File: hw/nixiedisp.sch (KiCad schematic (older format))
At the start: 55 parts, among them J1 12VDC IN, J2 USB_B_Micro, J3 AVR-ISP-6, J4 pwr sw, Q1 MMBTA55, Q2 IRF540N, U1 ATmega328P-AU, U10 IN14, U11 IN14, U12 IN14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

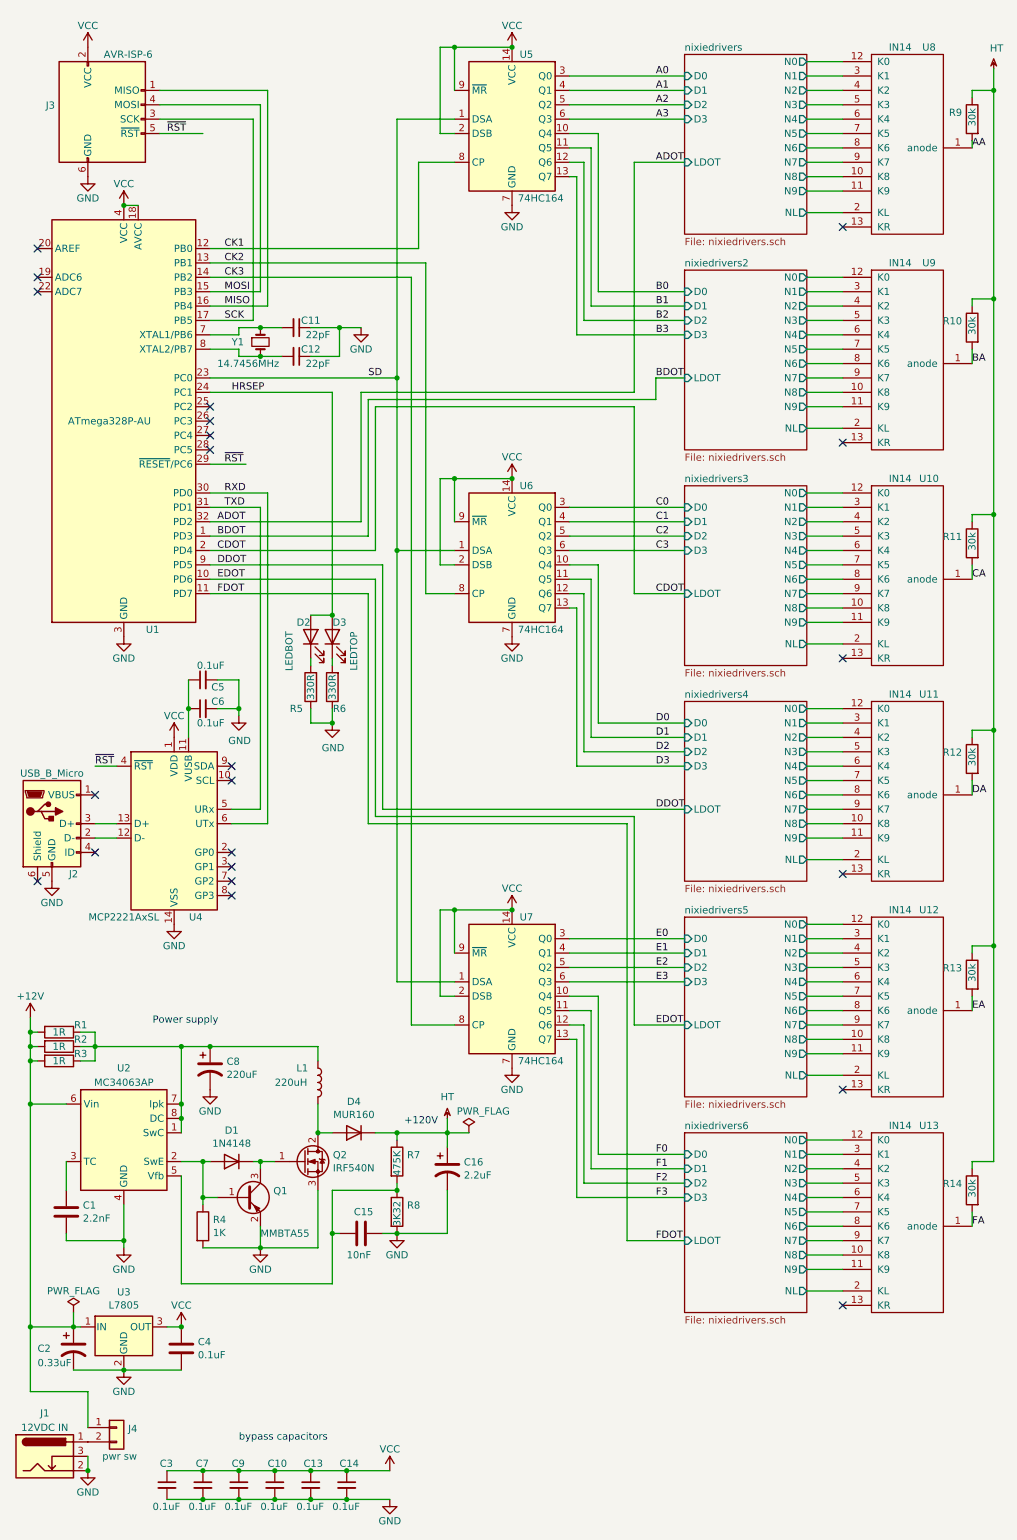
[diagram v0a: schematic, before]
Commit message: added RTC to the schematic
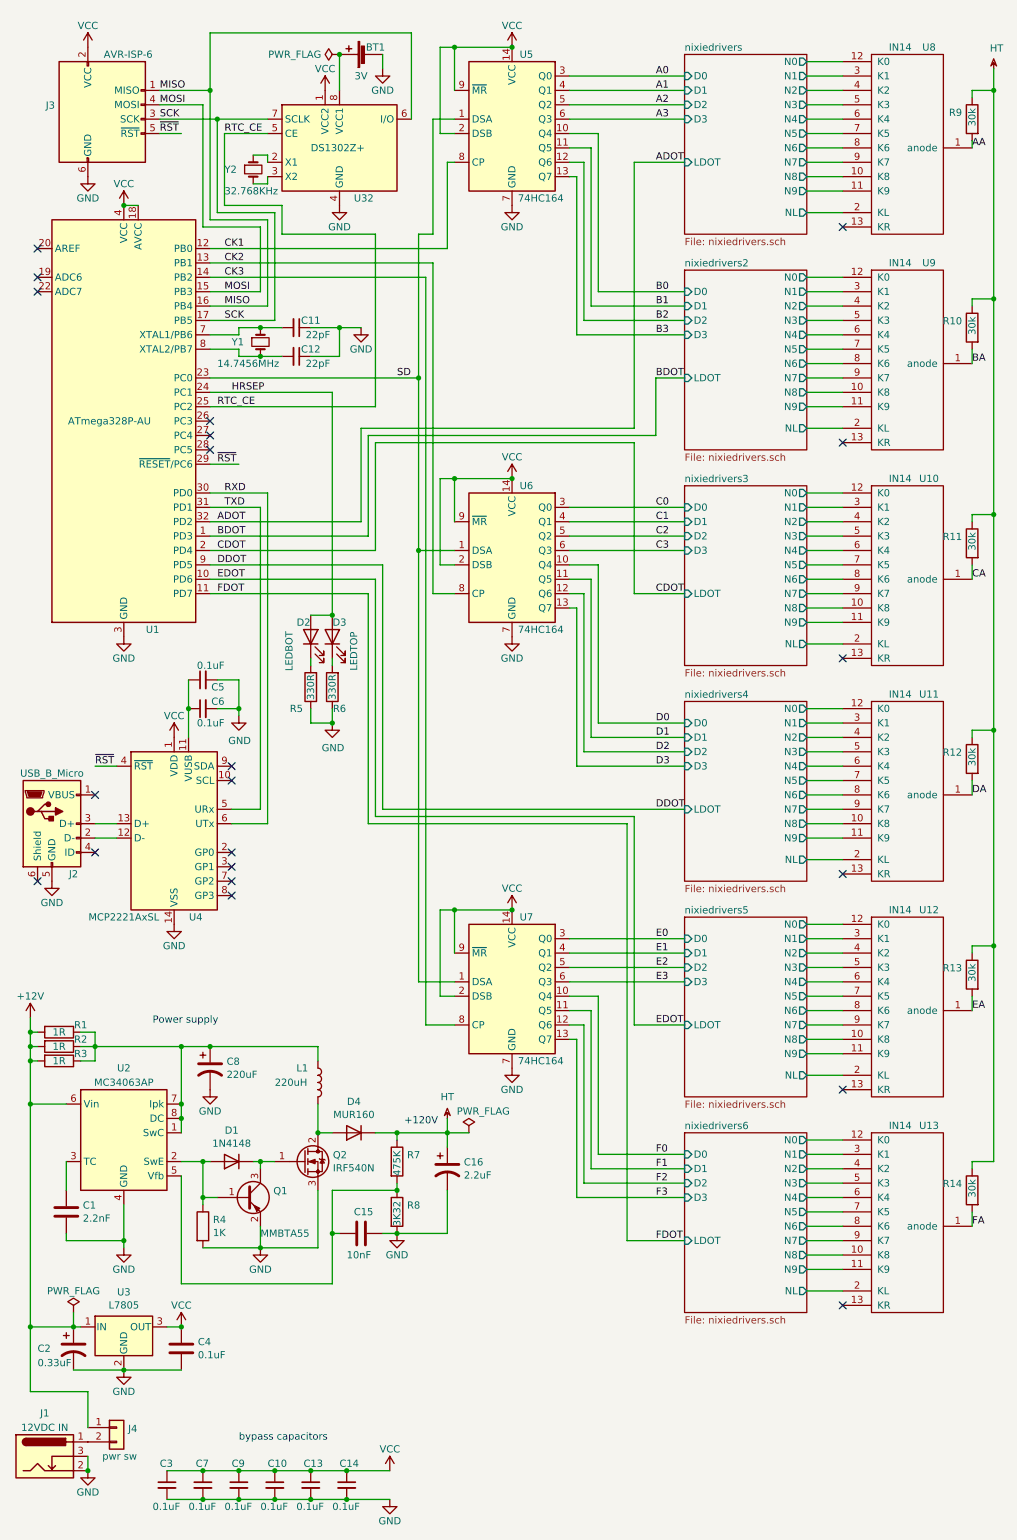
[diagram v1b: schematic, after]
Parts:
- added BT1: 3V, Battery:BatteryHolder_Keystone_1060_1x2032, symbol Device:Battery_Cell
- added U32: DS1302Z+, Package_SO:SOIC-8_3.9x4.9mm_P1.27mm, symbol Timer_RTC:DS1302Z+
- added Y2: 32.768KHz, Crystal:Crystal_SMD_2012-2Pin_2.0x1.2mm_HandSoldering, symbol Device:Crystal_Small
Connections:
- net GND: now also BT1.2 (-), U32.4 (GND)
- net MISO: now also U32.6 (I/O)
- net SCK: now also U32.7 (SCLK)
- net VCC: now also U32.1 (VCC2)
- net RTC_CE: now reaches U1.25 (PC2)
- net RTC_CE: now also U32.5 (CE)
- new net: U32.2 (X1), Y2.1
- new net: U32.3 (X2), Y2.2
- new net: BT1.1 (+), U32.8 (VCC1)
- no-connect marks 22 -> 21
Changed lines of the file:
@@
 Text Label 2150 2650 0    50   ~ 0
 MISO
-Wire Wire Line
-	2050 2750 2350 2750
 Text Label 2150 2750 0    50   ~ 0
 SCK
@@
 $EndComp
 Wire Wire Line
-	1700 1150 2450 1150
-Wire Wire Line
-	2450 1150 2450 2650
-Wire Wire Line
 	2050 2650 2450 2650
 Wire Wire Line
-	1700 1250 2400 1250
-Wire Wire Line
-	2400 1250 2400 2550
-Wire Wire Line
 	2050 2550 2400 2550
 Wire Wire Line
-	1700 1350 2350 1350
-Wire Wire Line
-	2350 1350 2350 2750
-Wire Wire Line
-	1700 1450 2000 1450
-Text Label 1750 1450 0    50   ~ 0
+	1700 1450 1850 1450
+Text Label 1700 1450 0    50   ~ 0
 ~RST
-Text Label 2150 3750 0    50   ~ 0
+Text Label 2100 3750 0    50   ~ 0
 ~RST
 $Comp
@@
 $EndComp
 Wire Wire Line
-	2050 2250 3500 2250
-Wire Wire Line
-	3500 2250 3500 1650
-Wire Wire Line
-	3500 1650 3750 1650
-Wire Wire Line
-	2050 2350 3550 2350
-Wire Wire Line
-	3550 2350 3550 4650
-Wire Wire Line
-	3550 4650 3750 4650
-Wire Wire Line
-	2050 2450 3450 2450
-Wire Wire Line
-	3450 2450 3450 7650
-Wire Wire Line
-	3450 7650 3750 7650
+	2050 2250 3700 2250
+Wire Wire Line
+	3700 2250 3700 1650
+Wire Wire Line
+	3700 1650 3750 1650
+Wire Wire Line
+	3600 2350 3600 4650
+Wire Wire Line
+	3600 4650 3750 4650
+Wire Wire Line
+	2050 2450 3550 2450
+Wire Wire Line
+	3550 2450 3550 7650
+Wire Wire Line
+	3550 7650 3750 7650
 Text Label 2150 2250 0    50   ~ 0
 CK1
@@
 TXD
 Wire Wire Line
-	3350 3150 3350 1350
-Wire Wire Line
-	3350 1350 3750 1350
-Wire Wire Line
-	3350 3150 3350 4350
-Wire Wire Line
-	3350 4350 3750 4350
-Connection ~ 3350 3150
-Wire Wire Line
-	3350 4350 3350 7350
-Wire Wire Line
-	3350 7350 3750 7350
-Connection ~ 3350 4350
-Text Label 3150 3150 0    50   ~ 0
+	3500 3150 3500 2150
+Wire Wire Line
+	3500 3150 3500 4350
+Wire Wire Line
+	3500 4350 3750 4350
+Connection ~ 3500 3150
+Wire Wire Line
+	3500 4350 3500 7350
+Wire Wire Line
+	3500 7350 3750 7350
+Connection ~ 3500 4350
+Text Label 3350 3150 0    50   ~ 0
 SD
 Wire Wire Line
@@
 Connection ~ 3750 6850
 Wire Wire Line
-	2050 3150 3350 3150
+	2050 3150 3500 3150
 Wire Wire Line
 	2950 2800 3100 2800
@@
 FDOT
 Wire Wire Line
-	3100 4150 3100 3250
-Wire Wire Line
-	3100 3250 5000 3250
-Wire Wire Line
-	5000 3250 5000 1650
+	3100 4150 3100 3500
+Wire Wire Line
+	3100 3500 5000 3500
+Wire Wire Line
+	5000 3500 5000 1650
 Wire Wire Line
 	5000 1650 5350 1650
@@
 	2050 4150 3100 4150
 Wire Wire Line
-	3150 4250 3150 3300
-Wire Wire Line
-	3150 3300 5150 3300
-Wire Wire Line
-	5150 3300 5150 3150
+	3150 4250 3150 3550
+Wire Wire Line
+	3150 3550 5150 3550
+Wire Wire Line
+	5150 3550 5150 3150
 Wire Wire Line
 	2050 4250 3150 4250
 Wire Wire Line
-	3200 4350 3200 3350
-Wire Wire Line
-	3200 3350 5000 3350
-Wire Wire Line
-	5000 3350 5000 4650
+	3200 4350 3200 3600
+Wire Wire Line
+	3200 3600 5000 3600
+Wire Wire Line
+	5000 3600 5000 4650
 Wire Wire Line
 	5000 4650 5350 4650
@@
 	2050 3950 2450 3950
 Wire Wire Line
-	2050 3750 2300 3750
+	2050 3750 2250 3750
 $Comp
 L Device:C_Small C6
@@
 	1    0    0    -1
 $EndComp
-NoConn ~ 2050 3350
 NoConn ~ 2050 3450
 NoConn ~ 2050 3550
@@
 Text Label 7350 9050 0    50   ~ 0
 FA
+$Comp
+L Timer_RTC:DS1302Z+ U32
+U 1 1 623FA4BC
+P 2950 1550
+F 0 "U32" H 3050 1200 50  0000 L CNN
+F 1 "DS1302Z+" H 2750 1550 50  0000 L CNN
+F 2 "Package_SO:SOIC-8_3.9x4.9mm_P1.27mm" H 2950 1050 50  0001 C CNN
+F 3 "https://datasheets.maximintegrated.com/en/ds/DS1302.pdf" H 2950 1550 50  0001 C CNN
+	1    2950 1550
+	1    0    0    -1
+$EndComp
+Wire Wire Line
+	2350 1800 2450 1800
+$Comp
+L power:GND #PWR0138
+U 1 1 62634E4F
+P 2950 1950
+F 0 "#PWR0138" H 2950 1700 50  0001 C CNN
+F 1 "GND" H 2950 1800 50  0000 C CNN
+F 2 "" H 2950 1950 50  0001 C CNN
+F 3 "" H 2950 1950 50  0001 C CNN
+	1    2950 1950
+	1    0    0    -1
+$EndComp
+Wire Wire Line
+	3450 1350 3450 750
+Wire Wire Line
+	3450 750  2050 750
+Wire Wire Line
+	1700 1350 2100 1350
+Wire Wire Line
+	2450 1800 2450 1750
+$Comp
+L Device:Crystal_Small Y2
+U 1 1 623FC7B6
+P 2350 1700
+F 0 "Y2" V 2350 1500 50  0000 L CNN
+F 1 "32.768KHz" V 2500 1500 50  0000 L CNN
+F 2 "Crystal:Crystal_SMD_2012-2Pin_2.0x1.2mm_HandSoldering" H 2350 1700 50  0001 C CNN
+F 3 "~" H 2350 1700 50  0001 C CNN
+F 4 "6pF" H 2350 1700 50  0001 C CNN "load"
+	1    2350 1700
+	0    1    1    0
+$EndComp
+Wire Wire Line
+	2350 1600 2450 1600
+Wire Wire Line
+	2450 1600 2450 1650
+Wire Wire Line
+	3500 2150 3600 2150
+Wire Wire Line
+	3600 2150 3600 1350
+Wire Wire Line
+	3600 1350 3750 1350
+Wire Wire Line
+	2400 2550 2400 2100
+Wire Wire Line
+	2400 2100 2000 2100
+Wire Wire Line
+	2000 2100 2000 1250
+Wire Wire Line
+	2000 1250 1700 1250
+Wire Wire Line
+	2450 2650 2450 2050
+Wire Wire Line
+	2450 2050 2050 2050
+Wire Wire Line
+	2050 2050 2050 1150
+Wire Wire Line
+	2050 1150 1700 1150
+Wire Wire Line
+	2050 2350 3600 2350
+Wire Wire Line
+	2500 2750 2500 2000
+Wire Wire Line
+	2500 2000 2100 2000
+Wire Wire Line
+	2100 2000 2100 1350
+Wire Wire Line
+	2050 2750 2500 2750
+Connection ~ 2100 1350
+Wire Wire Line
+	2100 1350 2450 1350
+$Comp
+L power:VCC #PWR0137
+U 1 1 62891898
+P 2850 1150
+F 0 "#PWR0137" H 2850 1000 50  0001 C CNN
+F 1 "VCC" H 2850 1300 50  0000 C CNN
+F 2 "" H 2850 1150 50  0001 C CNN
+F 3 "" H 2850 1150 50  0001 C CNN
+	1    2850 1150
+	1    0    0    -1
+$EndComp
+$Comp
+L Device:Battery_Cell BT1
+U 1 1 62892D7C
+P 3150 900
+F 0 "BT1" V 3200 850 50  0000 C CNN
+F 1 "3V" V 3000 950 50  0000 C CNN
+F 2 "Battery:BatteryHolder_Keystone_1060_1x2032" V 3150 960 50  0001 C CNN
+F 3 "~" V 3150 960 50  0001 C CNN
+	1    3150 900
+	0    -1   -1   0
+$EndComp
+$Comp
+L power:GND #PWR0139
+U 1 1 6289505D
+P 3250 1000
+F 0 "#PWR0139" H 3250 750 50  0001 C CNN
+F 1 "GND" H 3250 850 50  0000 C CNN
+F 2 "" H 3250 1000 50  0001 C CNN
+F 3 "" H 3250 1000 50  0001 C CNN
+	1    3250 1000
+	1    0    0    -1
+$EndComp
+Wire Wire Line
+	3250 900  3250 1000
+Wire Wire Line
+	2950 900  2950 1150
+Text Label 2100 3350 0    50   ~ 0
+RTC_CE
+Wire Wire Line
+	2450 1450 2150 1450
+Text Label 2150 1450 0    50   ~ 0
+RTC_CE
+Wire Wire Line
+	3200 3350 3200 2150
+Wire Wire Line
+	3200 2150 2550 2150
+Wire Wire Line
+	2550 2150 2550 1950
+Wire Wire Line
+	2550 1950 2150 1950
+Wire Wire Line
+	2150 1950 2150 1450
+Wire Wire Line
+	2050 3350 3200 3350
+Wire Wire Line
+	2050 750  2050 1150
+Connection ~ 2050 1150
+Text Label 1700 1150 0    50   ~ 0
+MISO
+Text Label 1700 1250 0    50   ~ 0
+MOSI
+Text Label 1700 1350 0    50   ~ 0
+SCK
+$Comp
+L power:PWR_FLAG #FLG0103
+U 1 1 62B59C57
+P 2950 900
+F 0 "#FLG0103" H 2950 975 50  0001 C CNN
+F 1 "PWR_FLAG" V 2950 1027 50  0000 L CNN
+F 2 "" H 2950 900 50  0001 C CNN
+F 3 "~" H 2950 900 50  0001 C CNN
+	1    2950 900
+	0    -1   -1   0
+$EndComp
+Connection ~ 2950 900
 $EndSCHEMATC

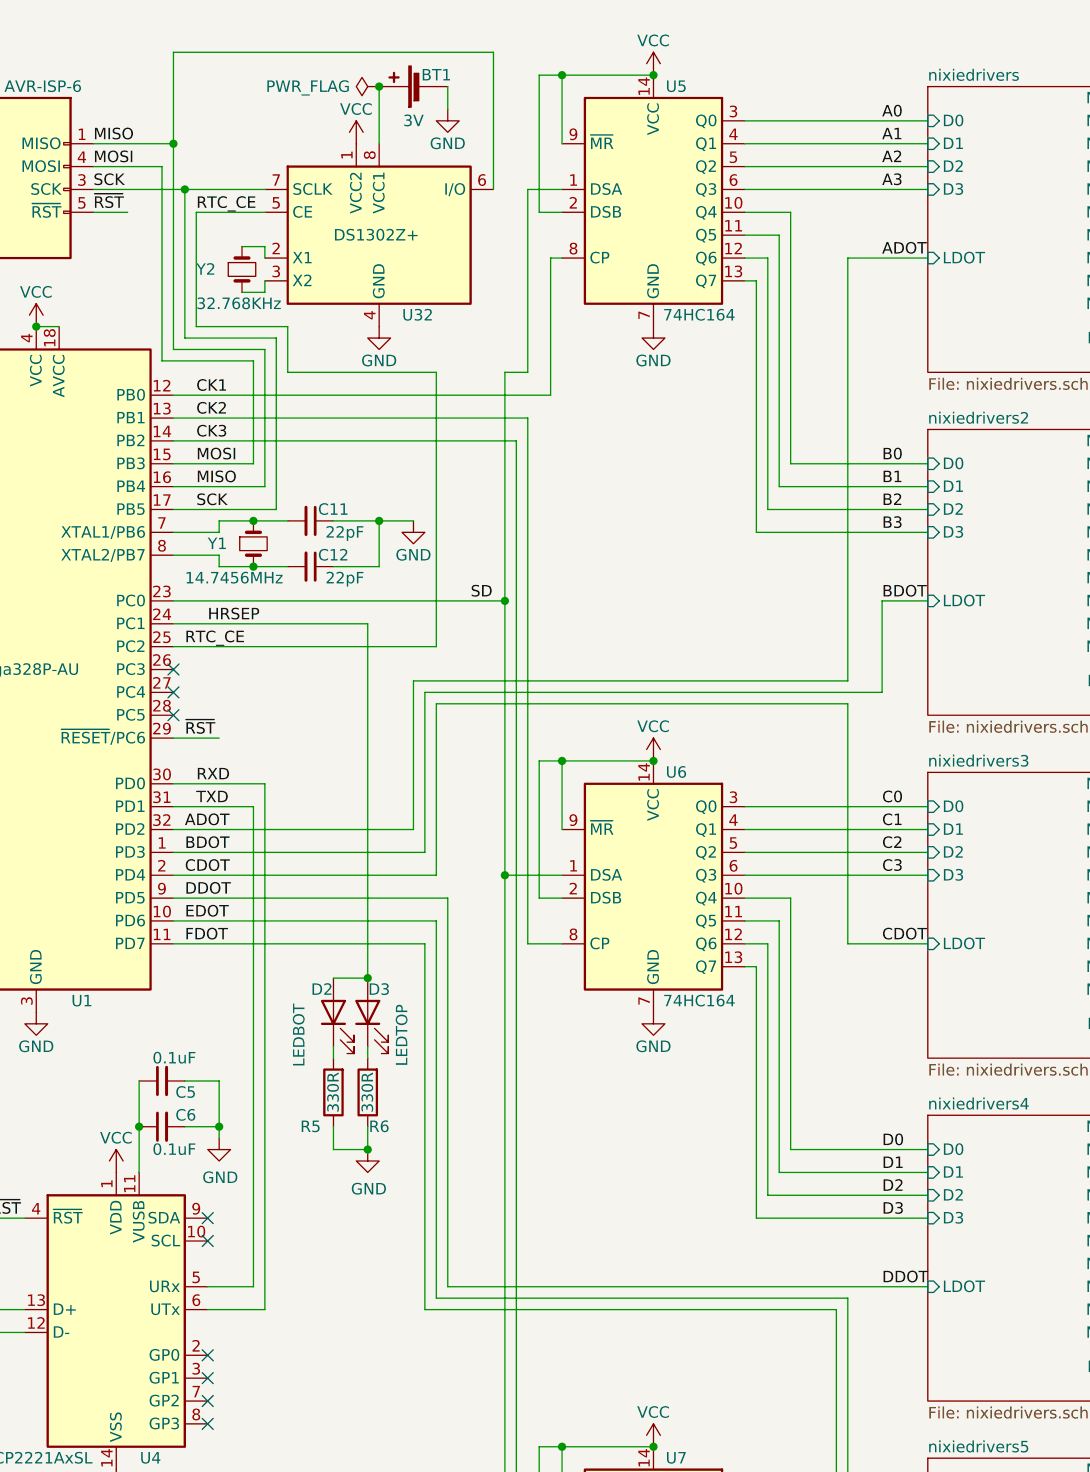
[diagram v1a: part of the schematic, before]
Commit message: PCB layout almost done
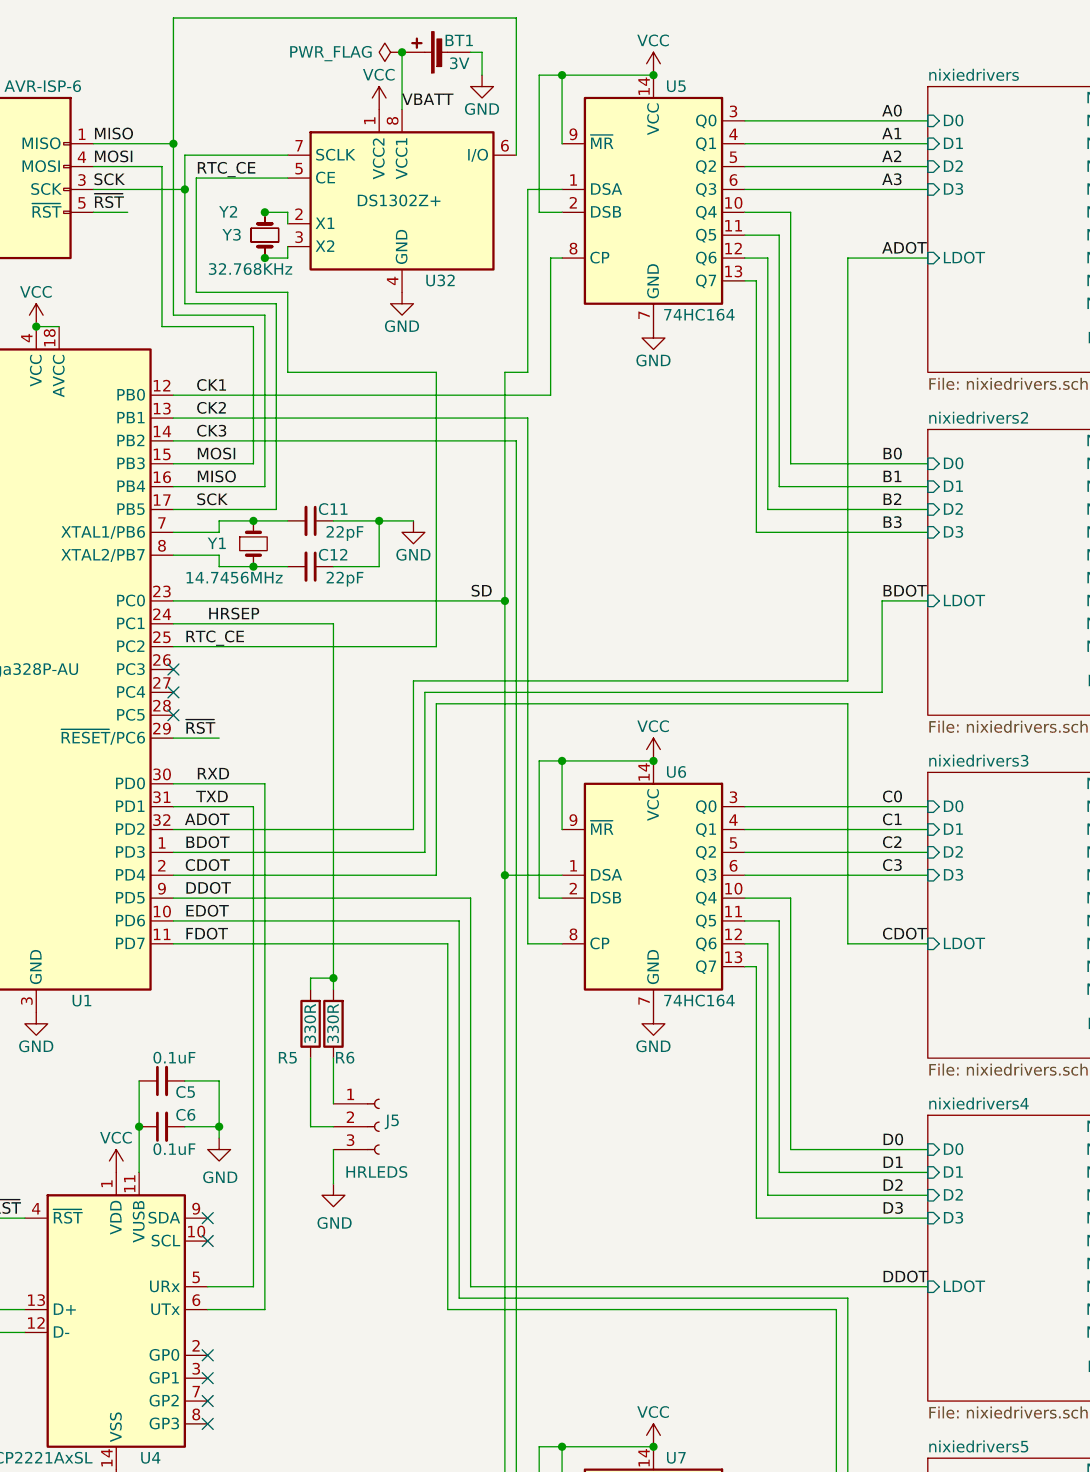
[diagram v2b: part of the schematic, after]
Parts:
- removed D2: LEDBOT, LED_SMD:LED_0805_2012Metric_Pad1.15x1.40mm_HandSolder, symbol Device:LED
- removed D3: LEDTOP, LED_SMD:LED_0805_2012Metric_Pad1.15x1.40mm_HandSolder, symbol Device:LED
- added J5: HRLEDS, Connector_PinSocket_2.54mm:PinSocket_1x03_P2.54mm_Vertical, symbol Connector:Conn_01x03_Female
- added Y3: 32.768KHz, Crystal:Crystal_C38-LF_D3.0mm_L8.0mm_Horizontal, symbol Device:Crystal_Small
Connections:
- net GND: now also J5.3 (Pin_3); no longer R5.1, R6.1
- net HRSEP: now also R5.2, R6.2
- net at U32.2 (X1), Y2.1: now also Y3.2
- net at U32.3 (X2), Y2.2: now also Y3.1
- net VBATT: now reaches BT1.1 (+), U32.8 (VCC1)
- new net: J5.1 (Pin_1), R6.1
- new net: J5.2 (Pin_2), R5.1
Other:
- moved on the sheet: BT1, R5, R6, U32, Y2
